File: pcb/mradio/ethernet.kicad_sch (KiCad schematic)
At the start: 28 parts, among them J301 JX0026D21BNL, U301 DP83825I, Y301 DSC1525JL2A-25M00000T

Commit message: make test points smaller
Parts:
- TP301, TP302, TP303, TP304, TP305, TP306, TP307: footprint TestPoint:TestPoint_Loop_D2.60mm_Drill0.9mm_Beaded -> TestPoint:TestPoint_Loop_D1.80mm_Drill1.0mm_Beaded
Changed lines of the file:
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@@
 			)
 		)
-		(property "Footprint" "TestPoint:TestPoint_Loop_D2.60mm_Drill0.9mm_Beaded"
+		(property "Footprint" "TestPoint:TestPoint_Loop_D1.80mm_Drill1.0mm_Beaded"
 			(at 90.17 171.45 0)
 			(hide yes)
@@
 			)
 		)
-		(property "Footprint" "TestPoint:TestPoint_Loop_D2.60mm_Drill0.9mm_Beaded"
+		(property "Footprint" "TestPoint:TestPoint_Loop_D1.80mm_Drill1.0mm_Beaded"
 			(at 115.57 96.52 0)
 			(hide yes)
@@
 			)
 		)
-		(property "Footprint" "TestPoint:TestPoint_Loop_D2.60mm_Drill0.9mm_Beaded"
+		(property "Footprint" "TestPoint:TestPoint_Loop_D1.80mm_Drill1.0mm_Beaded"
 			(at 106.68 81.28 0)
 			(hide yes)
@@
 			)
 		)
-		(property "Footprint" "TestPoint:TestPoint_Loop_D2.60mm_Drill0.9mm_Beaded"
+		(property "Footprint" "TestPoint:TestPoint_Loop_D1.80mm_Drill1.0mm_Beaded"
 			(at 116.84 78.74 0)
 			(hide yes)
@@
 			)
 		)
-		(property "Footprint" "TestPoint:TestPoint_Loop_D2.60mm_Drill0.9mm_Beaded"
+		(property "Footprint" "TestPoint:TestPoint_Loop_D1.80mm_Drill1.0mm_Beaded"
 			(at 175.26 132.08 0)
 			(hide yes)
@@
 			)
 		)
-		(property "Footprint" "TestPoint:TestPoint_Loop_D2.60mm_Drill0.9mm_Beaded"
+		(property "Footprint" "TestPoint:TestPoint_Loop_D1.80mm_Drill1.0mm_Beaded"
 			(at 105.41 99.06 0)
 			(hide yes)
@@
 			)
 		)
-		(property "Footprint" "TestPoint:TestPoint_Loop_D2.60mm_Drill0.9mm_Beaded"
+		(property "Footprint" "TestPoint:TestPoint_Loop_D1.80mm_Drill1.0mm_Beaded"
 			(at 96.52 129.54 0)
 			(hide yes)

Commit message: SDIO class and WiFi/mag jack layout
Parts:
- added C313: 1nF, 1KV, Capacitor_SMD:C_0603_1608Metric, symbol Device:C_Small
- added C314: skibidi farads, Capacitor_SMD:C_0603_1608Metric, symbol Device:C_Small
- added R306: 1M, Resistor_SMD:R_0603_1608Metric, symbol Device:R
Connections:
- net GND: now also C313.1, C314.2, R306.1; no longer J301.4 (CHS_GROUND_1), J301.5 (CHS_GROUND_2)
- net at J301.MH1: now also J301.MH2, C314.1
- new net: C313.2, J301.4 (CHS_GROUND_1), J301.5 (CHS_GROUND_2), R306.2
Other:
- moved on the sheet: J301, R305

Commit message: finished component placement
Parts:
- removed C313: 1nF, 1KV, Capacitor_SMD:C_0603_1608Metric, symbol Device:C_Small
- removed R306: 1M, Resistor_SMD:R_0603_1608Metric, symbol Device:R
- removed TP301, TP303, TP304, TP305, TP306, TP307: TestPoint, TestPoint:TestPoint_Loop_D1.80mm_Drill1.0mm_Beaded, symbol Connector:TestPoint
- C313: renamed from C314; value skibidi farads -> 0nF
- R305: value R -> 55
- renumbered MOSFET301 to Q301, TP302 to TP301
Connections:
- net GND: now also J301.4 (CHS_GROUND_1), J301.5 (CHS_GROUND_2)

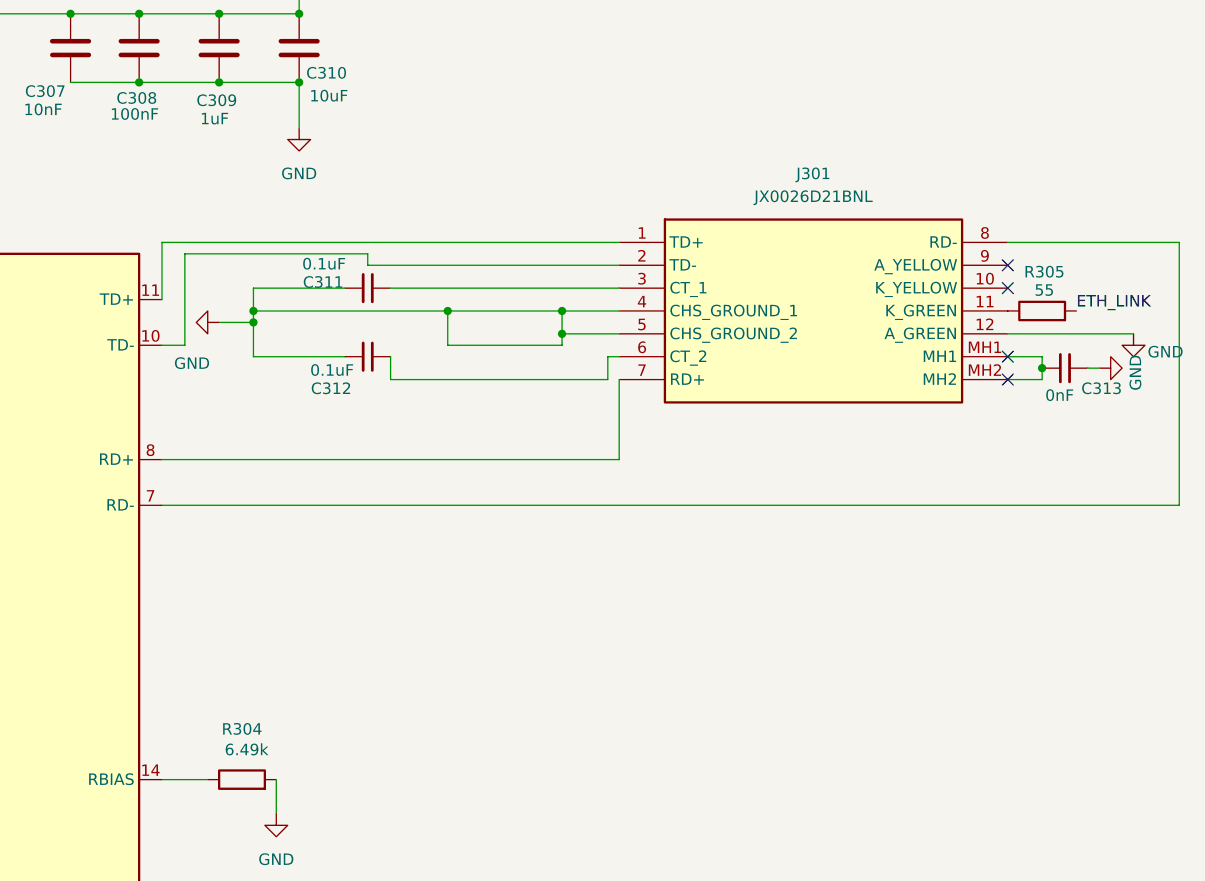
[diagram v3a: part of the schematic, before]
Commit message: changed eth magjack
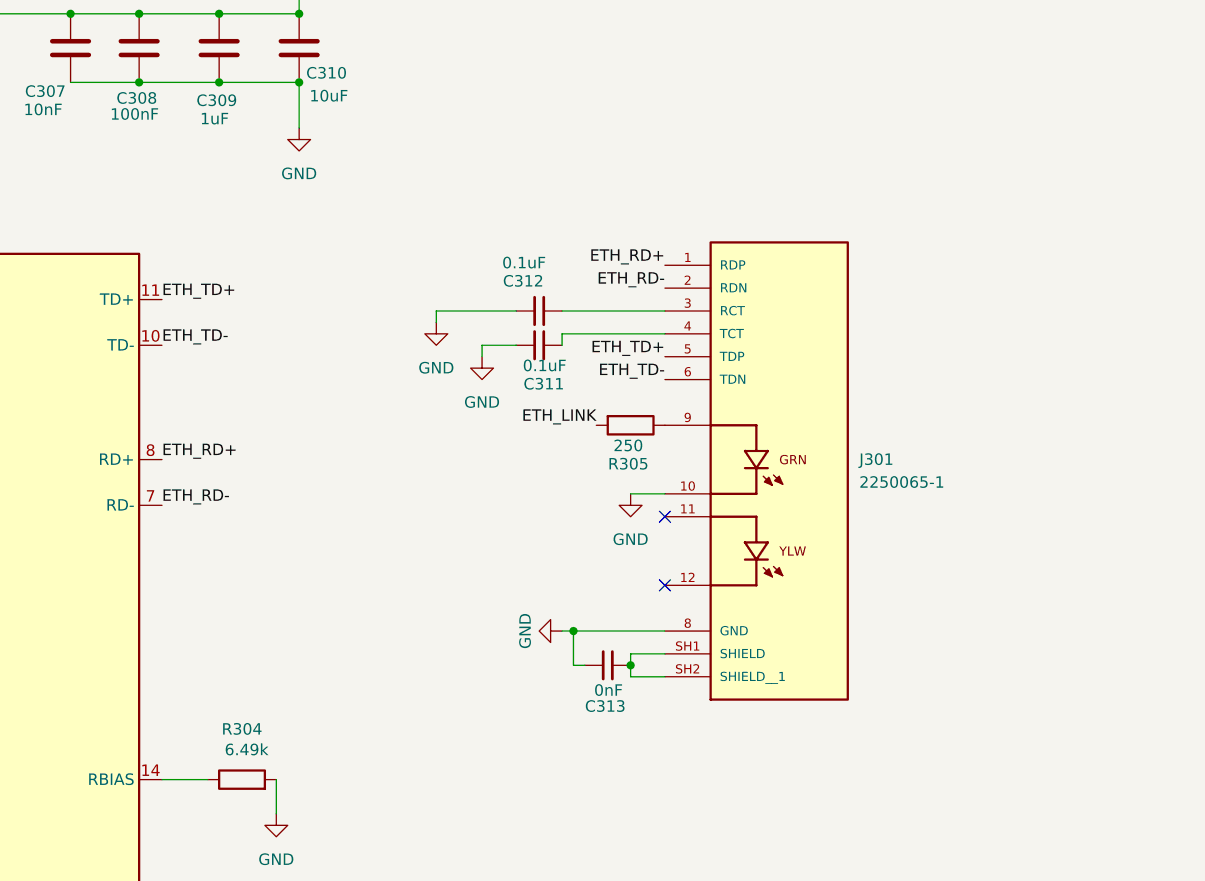
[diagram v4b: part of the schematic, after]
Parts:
- removed J301: JX0026D21BNL, JX0026D21BNL:JX0026D21BNL, symbol symbols:JX0026D21BNL
- added J301: 2250065-1, 2250065-1:BEL_2250065-1, symbol symbols:2250065-1
- R305: value 55 -> 250
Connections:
- net GND: now also J301.10, J301.8 (GND)
- net ETH_TD+: now reaches U301.11 (TD+)
- net ETH_TD+: now also J301.5 (TDP)
- net at R305.1: now also J301.9
- net ETH_TD-: now reaches U301.10 (TD-)
- net ETH_TD-: now also J301.6 (TDN)
- net at C311.2: now also J301.4 (TCT)
- net at C312.2: now also J301.3 (RCT)
- net ETH_RD+: now reaches U301.8 (RD+)
- net ETH_RD+: now also J301.1 (RDP)
- net ETH_RD-: now reaches U301.7 (RD-)
- net ETH_RD-: now also J301.2 (RDN)
- net at C313.1: now also J301.SH1 (SHIELD), J301.SH2 (SHIELD__1)
- no-connect marks 6 -> 4
